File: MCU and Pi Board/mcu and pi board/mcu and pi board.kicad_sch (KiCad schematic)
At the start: 1 part

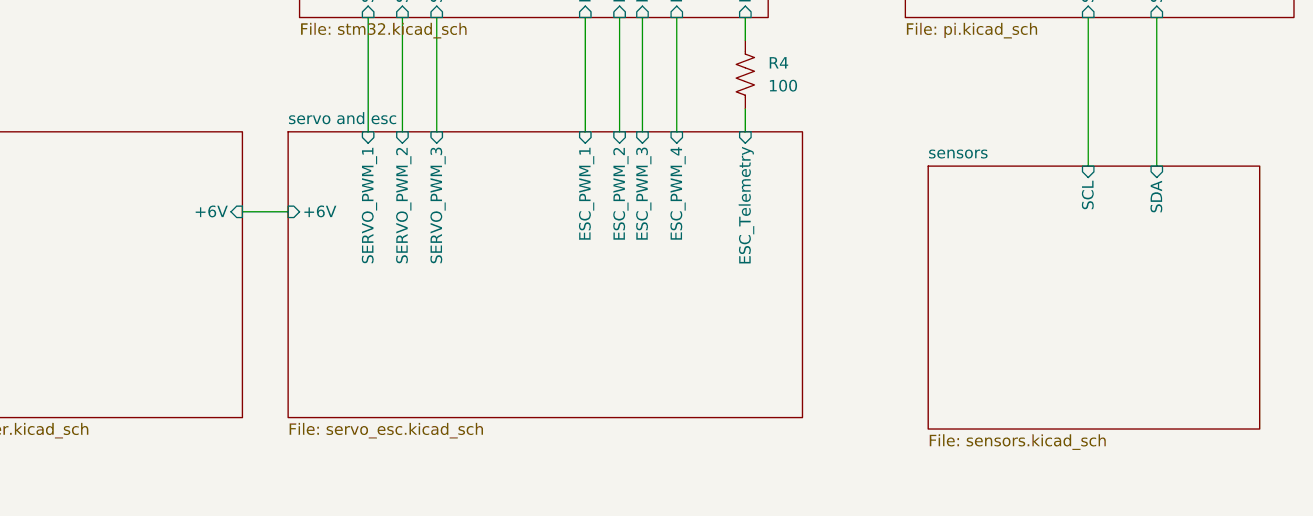
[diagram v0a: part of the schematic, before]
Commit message: added leds and minor fixes
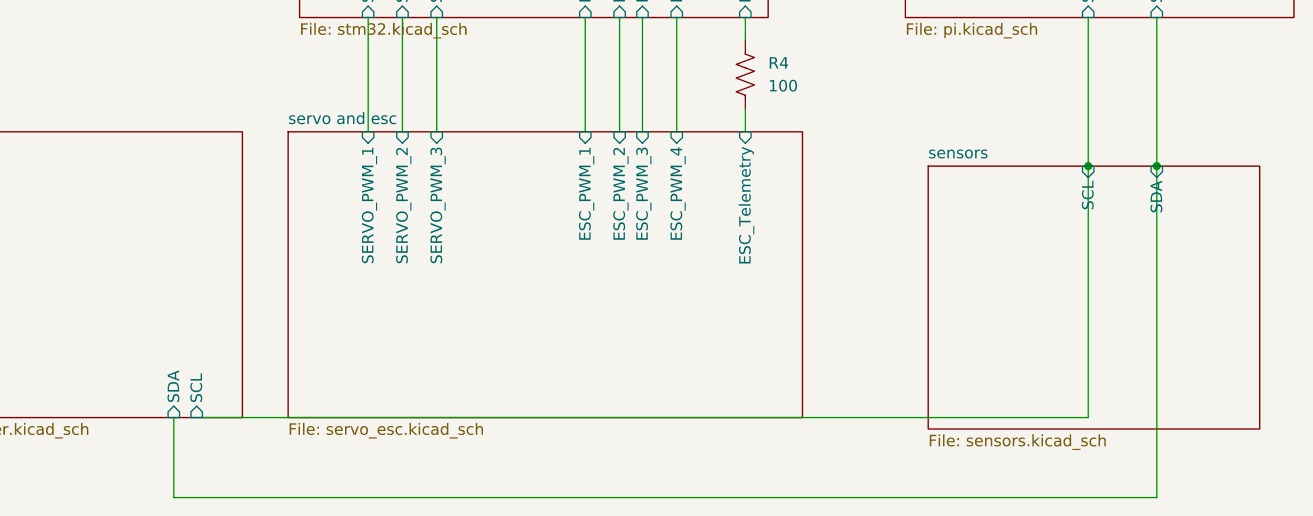
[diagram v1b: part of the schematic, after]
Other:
- sheet power ports: added SCL, SDA; removed +6V
- sheet servo and esc ports: added none; removed +6V
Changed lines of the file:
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@@
 	(generator_version "9.0")
 	(paper "A4")
+	(junction
+		(at 207.01 77.47)
+		(diameter 0)
+		(color 0 0 0 0)
+	)
+	(junction
+		(at 199.39 77.47)
+		(diameter 0)
+		(color 0 0 0 0)
+	)
 	(wire
 		(pts
@@
 	(wire
 		(pts
+			(xy 97.79 114.3) (xy 207.01 114.3)
+		)
+		(stroke
+			(width 0)
+			(type default)
+		)
+	)
+	(wire
+		(pts
 			(xy 161.29 60.96) (xy 161.29 63.5)
 		)
@@
 	(wire
 		(pts
-			(xy 105.41 82.55) (xy 110.49 82.55)
-		)
-		(stroke
-			(width 0)
-			(type default)
-		)
-	)
-	(wire
-		(pts
 			(xy 127 60.96) (xy 127 73.66)
 		)
@@
 	(wire
 		(pts
+			(xy 100.33 105.41) (xy 199.39 105.41)
+		)
+		(stroke
+			(width 0)
+			(type default)
+		)
+	)
+	(wire
+		(pts
+			(xy 207.01 114.3) (xy 207.01 77.47)
+		)
+		(stroke
+			(width 0)
+			(type default)
+		)
+	)
+	(wire
+		(pts
 			(xy 147.32 60.96) (xy 147.32 73.66)
+		)
+		(stroke
+			(width 0)
+			(type default)
+		)
+	)
+	(wire
+		(pts
+			(xy 199.39 105.41) (xy 199.39 77.47)
+		)
+		(stroke
+			(width 0)
+			(type default)
+		)
+	)
+	(wire
+		(pts
+			(xy 97.79 105.41) (xy 97.79 114.3)
 		)
 		(stroke
@@
 			)
 		)
-		(pin "+6V" input
-			(at 105.41 82.55 0)
-			(effects
-				(font
-					(size 1.27 1.27)
-				)
-				(justify right)
+		(pin "SCL" input
+			(at 100.33 105.41 270)
+			(effects
+				(font
+					(size 1.27 1.27)
+				)
+				(justify left)
+			)
+		)
+		(pin "SDA" input
+			(at 97.79 105.41 270)
+			(effects
+				(font
+					(size 1.27 1.27)
+				)
+				(justify left)
 			)
 		)
@@
 			)
 		)
-		(pin "+6V" input
-			(at 110.49 82.55 180)
-			(effects
-				(font
-					(size 1.27 1.27)
-				)
-				(justify left)
-			)
-		)

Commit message: minor edits
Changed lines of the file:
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@@
+	(wire
+		(pts
+			(xy 97.79 114.3) (xy 207.01 114.3)
+		)
+		(stroke
+			(width 0)
+			(type default)
+		)
+	)
+	(wire
+		(pts
+			(xy 161.29 60.96) (xy 161.29 63.5)
+		)
+		(stroke
+			(width 0)
+			(type default)
+		)
+	)
+	(wire
+		(pts
+			(xy 153.67 60.96) (xy 153.67 73.66)
+		)
+		(stroke
+			(width 0)
+			(type default)
+		)
+	)
+	(wire
+		(pts
+			(xy 143.51 60.96) (xy 143.51 73.66)
+		)
+		(stroke
+			(width 0)
+			(type default)
+		)
+	)
+	(wire
+		(pts
+			(xy 207.01 60.96) (xy 207.01 77.47)
+		)
+		(stroke
+			(width 0)
+			(type default)
+		)
+	)
+	(wire
+		(pts
+			(xy 163.83 41.91) (xy 179.07 41.91)
+		)
+		(stroke
+			(width 0)
+			(type default)
+		)
+	)
 	(wire
 		(pts
@@
 	(wire
 		(pts
-			(xy 97.79 114.3) (xy 207.01 114.3)
-		)
-		(stroke
-			(width 0)
-			(type default)
-		)
-	)
-	(wire
-		(pts
-			(xy 161.29 60.96) (xy 161.29 63.5)
-		)
-		(stroke
-			(width 0)
-			(type default)
-		)
-	)
-	(wire
-		(pts
-			(xy 153.67 60.96) (xy 153.67 73.66)
-		)
-		(stroke
-			(width 0)
-			(type default)
-		)
-	)
-	(wire
-		(pts
-			(xy 143.51 60.96) (xy 143.51 73.66)
-		)
-		(stroke
-			(width 0)
-			(type default)
-		)
-	)
-	(wire
-		(pts
-			(xy 207.01 60.96) (xy 207.01 77.47)
-		)
-		(stroke
-			(width 0)
-			(type default)
-		)
-	)
-	(wire
-		(pts
-			(xy 163.83 41.91) (xy 179.07 41.91)
-		)
-		(stroke
-			(width 0)
-			(type default)
-		)
-	)
-	(wire
-		(pts
 			(xy 199.39 60.96) (xy 199.39 77.47)
 		)
@@
 	(wire
 		(pts
-			(xy 100.33 105.41) (xy 199.39 105.41)
+			(xy 100.33 111.76) (xy 199.39 111.76)
+		)
+		(stroke
+			(width 0)
+			(type default)
+		)
+	)
+	(wire
+		(pts
+			(xy 163.83 33.02) (xy 179.07 33.02)
 		)
 		(stroke
@@
 	(wire
 		(pts
-			(xy 199.39 105.41) (xy 199.39 77.47)
+			(xy 199.39 111.76) (xy 199.39 77.47)
 		)
 		(stroke
@@
 	(wire
 		(pts
-			(xy 163.83 31.75) (xy 179.07 31.75)
-		)
-		(stroke
-			(width 0)
-			(type default)
-		)
-	)
-	(wire
-		(pts
 			(xy 123.19 60.96) (xy 123.19 73.66)
 		)
@@
 		(pts
 			(xy 163.83 39.37) (xy 179.07 39.37)
+		)
+		(stroke
+			(width 0)
+			(type default)
+		)
+	)
+	(wire
+		(pts
+			(xy 100.33 105.41) (xy 100.33 111.76)
 		)
 		(stroke
@@
 		)
 		(pin "MISO" input
-			(at 163.83 31.75 0)
+			(at 163.83 35.56 0)
 			(effects
 				(font
@@
 		)
 		(pin "MOSI" input
-			(at 163.83 35.56 0)
+			(at 163.83 33.02 0)
 			(effects
 				(font
@@
 		)
 		(pin "MOSI" input
-			(at 179.07 31.75 180)
-			(effects
-				(font
+			(at 179.07 33.02 180)
+			(effects
+				(font

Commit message: pretty much done
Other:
- sheet STM32 renamed MCU
- sheet MCU ports: added RP2350B_CS, RP2350B_ESC_PWM_0, RP2350B_ESC_PWM_1, RP2350B_ESC_PWM_2, RP2350B_ESC_PWM_3, RP2350B_SERVO_PWM_0, RP2350B_SERVO_PWM_1, RP2350B_SERVO_PWM_2, SCL, SDA, STM_CS, STM_ESC_PWM_0, STM_ESC_PWM_1, STM_ESC_PWM_2, STM_ESC_PWM_3, STM_SERVO_PWM_0, STM_SERVO_PWM_1, STM_SERVO_PWM_2; removed ESC_PWM_1, ESC_PWM_2, ESC_PWM_3, ESC_PWM_4, NSS, SERVO_PWM_1, SERVO_PWM_2, SERVO_PWM_3
- sheet pi ports: added RP2350B_CS, STM_CS; removed NSS
- sheet servo and esc ports: added RP2350B_ESC_PWM_0, RP2350B_ESC_PWM_1, RP2350B_ESC_PWM_2, RP2350B_ESC_PWM_3, RP2350B_SERVO_PWM_0, RP2350B_SERVO_PWM_1, RP2350B_SERVO_PWM_2, STM_ESC_PWM_0, STM_ESC_PWM_1, STM_ESC_PWM_2, STM_ESC_PWM_3, STM_SERVO_PWM_0, STM_SERVO_PWM_1, STM_SERVO_PWM_2; removed ESC_PWM_1, ESC_PWM_2, ESC_PWM_3, ESC_PWM_4, SERVO_PWM_1, SERVO_PWM_2, SERVO_PWM_3
- moved on the sheet: R4

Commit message: started routing
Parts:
- R4: footprint (none) -> Resistor_SMD:R_0603_1608Metric_Pad0.98x0.95mm_HandSolder
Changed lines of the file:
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@@
 			)
 		)
-		(property "Footprint" ""
+		(property "Footprint" "Resistor_SMD:R_0603_1608Metric_Pad0.98x0.95mm_HandSolder"
 			(at 157.226 67.564 90)
 			(effects

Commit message: basically done
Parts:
- renumbered R4 to R15
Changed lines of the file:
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@@
 		(dnp no)
 		(fields_autoplaced yes)
-		(property "Reference" "R4"
+		(property "Reference" "R15"
 			(at 158.75 66.0399 0)
 			(effects
@@
 			(project ""
 				(path "/b20a486a-db1b-4621-abfe-a5d205c676b3"
-					(reference "R4")
+					(reference "R15")
 					(unit 1)
 				)
